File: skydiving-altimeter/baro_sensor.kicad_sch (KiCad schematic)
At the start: 5 parts, among them U2 BMP581

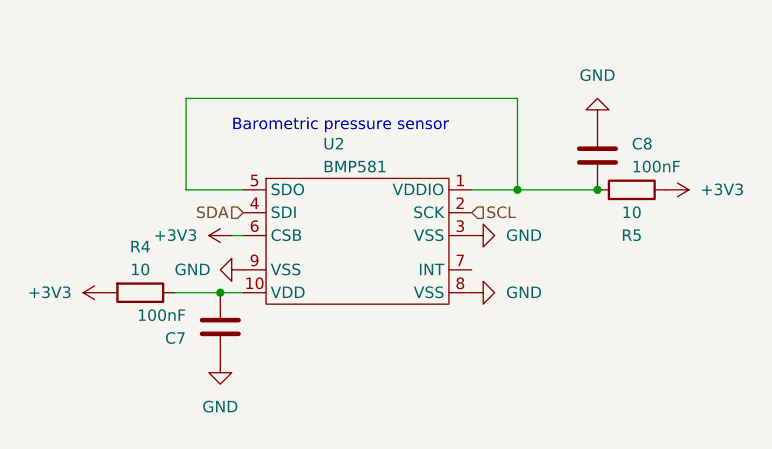
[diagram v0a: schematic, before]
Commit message: Switched from the bmp to the lps. Added usb port
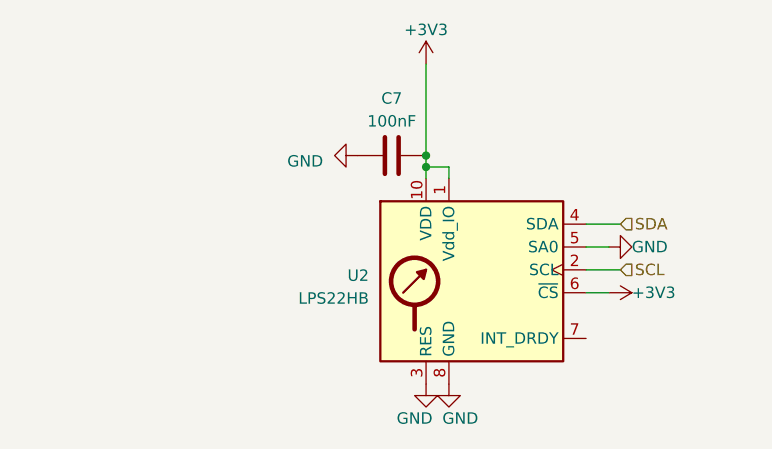
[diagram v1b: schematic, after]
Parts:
- removed C8: 100nF, Capacitor_SMD:C_0805_2012Metric, symbol Device:C
- removed R4, R5: 10, Resistor_SMD:R_0402_1005Metric, symbol Device:R
- removed U2: BMP581, BMP581:BMP581, symbol BMP581:BMP581
- added U2: LPS22HB, Package_LGA:ST_HLGA-10_2x2mm_P0.5mm_LayoutBorder3x2y, symbol Sensor_Pressure:LPS22HB
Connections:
- net +3V3: now also C7.1, U2.1 (Vdd_IO), U2.10 (VDD), U2.6 (~{CS})
- net GND: now also C7.2, U2.3 (RES), U2.5 (SA0), U2.8 (GND), U2.9 (GND); no longer C7.1
- net SCL: now also U2.2 (SCL)
- net SDA: now also U2.4 (SDA)
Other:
- note removed: "Barometric pressure sensor"
